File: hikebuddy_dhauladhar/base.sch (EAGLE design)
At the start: 114 parts, among them J1 MF-CON-MICROUSB-RIGHT, J2 GPS Port, J5 SOLDER_PAD_2, J9 47352-1001, U1 LTC3586EUFE-1#PBF, U2 MAX17260SETD+, U3 MF-DSC-SOT233-MMBT3904, U4 MF-DSC-SOT233-MMBT3904, U5 DRV2605LTDGSRQ1, U6 BMX160

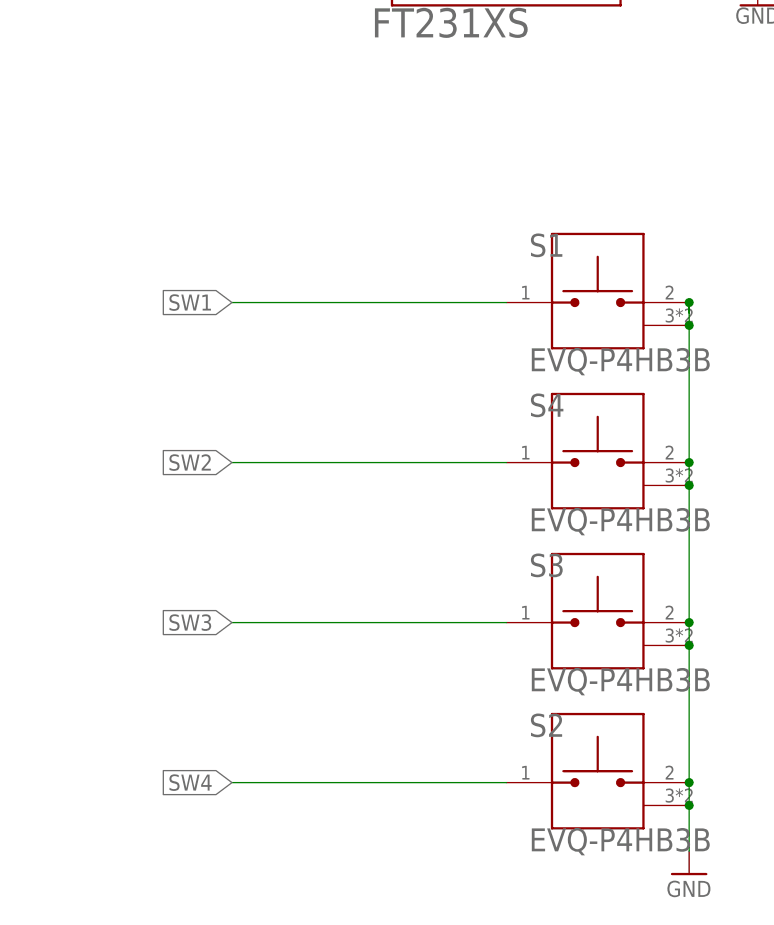
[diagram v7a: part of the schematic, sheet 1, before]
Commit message: added pullups to buttons, moved jst2 to make room for connector, removed test pads and joined EN to Vreg
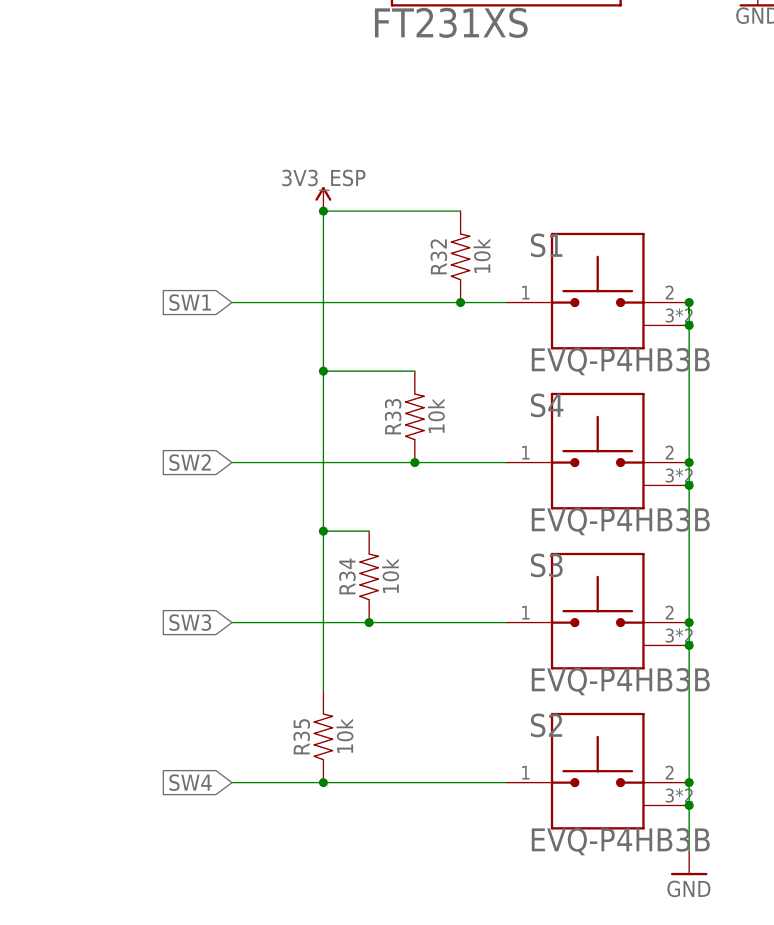
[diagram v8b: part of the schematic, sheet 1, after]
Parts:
- removed TP1, TP2: TEST-POINT2, SparkFun-Connectors:TEST-POINT2
- added R32, R33, R34, R35: 10k, SparkFun-Resistors:10KOHM-0603-1/10W-1%
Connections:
- removed net N$24: C20.P$2, R16.P$2, TP1.1, U1.FAULT
- net N$19: now also C20.P$2, R16.P$2, U1.FAULT; no longer TP2.1
- net SW1: now also R32.1
- net SW2: now also R33.1
- net SW3: now also R34.1
- net SW4: now also R35.1
- net VCC: now also R32.2, R33.2, R34.2, R35.2
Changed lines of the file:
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@@
 <part name="S1" library="EVQ-P4HB3B" deviceset="EVQ-P4HB3B" device="" override_package3d_urn="urn:adsk.eagle:package:16346036/2" override_package_urn="urn:adsk.eagle:footprint:16346037/1" override_locally_modified="yes"/>
 <part name="GND9" library="supply1" library_urn="urn:adsk.eagle:library:371" deviceset="GND" device=""/>
-<part name="TP1" library="SparkFun-Connectors" deviceset="TEST-POINT" device="2"/>
-<part name="TP2" library="SparkFun-Connectors" deviceset="TEST-POINT" device="2"/>
 <part name="J9" library="47352-1001" deviceset="47352-1001" device="" package3d_urn="urn:adsk.eagle:package:16346114/2"/>
+<part name="R32" library="SparkFun-Resistors" deviceset="10KOHM" device="-0603-1/10W-1%" package3d_urn="urn:adsk.eagle:package:23555/3" value="10k"/>
+<part name="R33" library="SparkFun-Resistors" deviceset="10KOHM" device="-0603-1/10W-1%" package3d_urn="urn:adsk.eagle:package:23555/3" value="10k"/>
+<part name="R34" library="SparkFun-Resistors" deviceset="10KOHM" device="-0603-1/10W-1%" package3d_urn="urn:adsk.eagle:package:23555/3" value="10k"/>
+<part name="R35" library="SparkFun-Resistors" deviceset="10KOHM" device="-0603-1/10W-1%" package3d_urn="urn:adsk.eagle:package:23555/3" value="10k"/>
+<part name="3V3_ESP3" library="SparkFun-PowerSymbols" library_urn="urn:adsk.eagle:library:530" deviceset="VCC" device="" value="3V3_ESP"/>
 </parts>
 <sheets>
@@
 <attribute name="NAME" x="350.52" y="168.402" size="1.778" layer="95"/>
 <attribute name="VALUE" x="350.52" y="134.62" size="1.778" layer="96"/>
+</instance>
+<instance part="R32" gate="G$1" x="53.34" y="27.94" smashed="yes" rot="R90">
+<attribute name="NAME" x="51.816" y="27.94" size="1.778" layer="95" font="vector" rot="R90" align="bottom-center"/>
+<attribute name="VALUE" x="54.864" y="27.94" size="1.778" layer="96" font="vector" rot="R90" align="top-center"/>
+</instance>
+<instance part="R33" gate="G$1" x="48.26" y="10.16" smashed="yes" rot="R90">
+<attribute name="NAME" x="46.736" y="10.16" size="1.778" layer="95" font="vector" rot="R90" align="bottom-center"/>
+<attribute name="VALUE" x="49.784" y="10.16" size="1.778" layer="96" font="vector" rot="R90" align="top-center"/>
+</instance>
+<instance part="R34" gate="G$1" x="43.18" y="-7.62" smashed="yes" rot="R90">
+<attribute name="NAME" x="41.656" y="-7.62" size="1.778" layer="95" font="vector" rot="R90" align="bottom-center"/>
+<attribute name="VALUE" x="44.704" y="-7.62" size="1.778" layer="96" font="vector" rot="R90" align="top-center"/>
+</instance>
+<instance part="R35" gate="G$1" x="38.1" y="-25.4" smashed="yes" rot="R90">
+<attribute name="NAME" x="36.576" y="-25.4" size="1.778" layer="95" font="vector" rot="R90" align="bottom-center"/>
+<attribute name="VALUE" x="39.624" y="-25.4" size="1.778" layer="96" font="vector" rot="R90" align="top-center"/>
+</instance>
+<instance part="3V3_ESP3" gate="G$1" x="38.1" y="33.02" smashed="yes">
+<attribute name="VALUE" x="38.1" y="35.814" size="1.778" layer="96" align="bottom-center"/>
 </instance>
 </instances>
@@
 <pinref part="C21" gate="G$1" pin="1"/>
 <junction x="403.86" y="114.3"/>
+</segment>
+<segment>
+<pinref part="R35" gate="G$1" pin="2"/>
+<wire x1="38.1" y1="-20.32" x2="38.1" y2="-2.54" width="0.1524" layer="91"/>
+<pinref part="R32" gate="G$1" pin="2"/>
+<wire x1="38.1" y1="-2.54" x2="38.1" y2="15.24" width="0.1524" layer="91"/>
+<wire x1="38.1" y1="15.24" x2="38.1" y2="33.02" width="0.1524" layer="91"/>
+<wire x1="38.1" y1="33.02" x2="53.34" y2="33.02" width="0.1524" layer="91"/>
+<pinref part="R33" gate="G$1" pin="2"/>
+<wire x1="48.26" y1="15.24" x2="38.1" y2="15.24" width="0.1524" layer="91"/>
+<junction x="38.1" y="15.24"/>
+<pinref part="R34" gate="G$1" pin="2"/>
+<wire x1="43.18" y1="-2.54" x2="38.1" y2="-2.54" width="0.1524" layer="91"/>
+<junction x="38.1" y="-2.54"/>
+<pinref part="3V3_ESP3" gate="G$1" pin="VCC"/>
+<junction x="38.1" y="33.02"/>
 </segment>
 </net>
@@
 <net name="SW1" class="0">
 <segment>
-<wire x1="58.42" y1="22.86" x2="27.94" y2="22.86" width="0.1524" layer="91"/>
+<wire x1="58.42" y1="22.86" x2="53.34" y2="22.86" width="0.1524" layer="91"/>
 <label x="27.94" y="22.86" size="1.778" layer="95" rot="R180" xref="yes"/>
 <pinref part="S1" gate="G$1" pin="1"/>
+<pinref part="R32" gate="G$1" pin="1"/>
+<wire x1="53.34" y1="22.86" x2="27.94" y2="22.86" width="0.1524" layer="91"/>
+<junction x="53.34" y="22.86"/>
 </segment>
 <segment>
@@
 <net name="SW2" class="0">
 <segment>
-<wire x1="58.42" y1="5.08" x2="27.94" y2="5.08" width="0.1524" layer="91"/>
+<wire x1="58.42" y1="5.08" x2="48.26" y2="5.08" width="0.1524" layer="91"/>
 <label x="27.94" y="5.08" size="1.778" layer="95" rot="R180" xref="yes"/>
 <pinref part="S4" gate="G$1" pin="1"/>
+<pinref part="R33" gate="G$1" pin="1"/>
+<wire x1="48.26" y1="5.08" x2="27.94" y2="5.08" width="0.1524" layer="91"/>
+<junction x="48.26" y="5.08"/>
 </segment>
 <segment>
@@
 <net name="SW3" class="0">
 <segment>
-<wire x1="58.42" y1="-12.7" x2="27.94" y2="-12.7" width="0.1524" layer="91"/>
+<wire x1="58.42" y1="-12.7" x2="43.18" y2="-12.7" width="0.1524" layer="91"/>
 <label x="27.94" y="-12.7" size="1.778" layer="95" rot="R180" xref="yes"/>
 <pinref part="S3" gate="G$1" pin="1"/>
+<pinref part="R34" gate="G$1" pin="1"/>
+<wire x1="43.18" y1="-12.7" x2="27.94" y2="-12.7" width="0.1524" layer="91"/>
+<junction x="43.18" y="-12.7"/>
 </segment>
 <segment>
@@
 <net name="SW4" class="0">
 <segment>
-<wire x1="58.42" y1="-30.48" x2="27.94" y2="-30.48" width="0.1524" layer="91"/>
+<wire x1="58.42" y1="-30.48" x2="38.1" y2="-30.48" width="0.1524" layer="91"/>
 <label x="27.94" y="-30.48" size="1.778" layer="95" rot="R180" xref="yes"/>
 <pinref part="S2" gate="G$1" pin="1"/>
+<pinref part="R35" gate="G$1" pin="1"/>
+<wire x1="38.1" y1="-30.48" x2="27.94" y2="-30.48" width="0.1524" layer="91"/>
+<junction x="38.1" y="-30.48"/>
 </segment>
 <segment>
@@
 <attribute name="NAME" x="48.26" y="64.516" size="1.016" layer="95" font="vector" rot="R180" align="top-left"/>
 <attribute name="VALUE" x="48.26" y="67.564" size="1.016" layer="96" font="vector" rot="R180"/>
-</instance>
-<instance part="TP1" gate="G$1" x="78.74" y="88.9" smashed="yes">
-<attribute name="NAME" x="76.2" y="91.44" size="1.778" layer="95" font="vector"/>
-<attribute name="VALUE" x="76.2" y="86.36" size="1.778" layer="96" font="vector"/>
-</instance>
-<instance part="TP2" gate="G$1" x="86.36" y="88.9" smashed="yes" rot="R180">
-<attribute name="NAME" x="88.9" y="86.36" size="1.778" layer="95" font="vector" rot="R180"/>
-<attribute name="VALUE" x="88.9" y="91.44" size="1.778" layer="96" font="vector" rot="R180"/>
 </instance>
 </instances>
@@
 </segment>
 </net>
-<net name="N$24" class="0">
-<segment>
+<net name="N$19" class="0">
+<segment>
+<pinref part="U1" gate="G$1" pin="EN3"/>
+<pinref part="U1" gate="G$1" pin="FAULT"/>
 <wire x1="78.74" y1="88.9" x2="78.74" y2="83.82" width="0.1524" layer="91"/>
-<pinref part="U1" gate="G$1" pin="FAULT"/>
 <wire x1="78.74" y1="83.82" x2="58.42" y2="83.82" width="0.1524" layer="91"/>
 <pinref part="R16" gate="G$1" pin="P$2"/>
@@
 <wire x1="53.34" y1="83.82" x2="50.8" y2="83.82" width="0.1524" layer="91"/>
 <junction x="53.34" y="83.82"/>
-<pinref part="TP1" gate="G$1" pin="1"/>
-</segment>
-</net>
-<net name="N$19" class="0">
-<segment>
-<pinref part="U1" gate="G$1" pin="EN3"/>
-<pinref part="TP2" gate="G$1" pin="1"/>
-<wire x1="86.36" y1="88.9" x2="93.98" y2="88.9" width="0.1524" layer="91"/>
-</segment>
-</net>
+<wire x1="93.98" y1="88.9" x2="78.74" y2="88.9" width="0.1524" layer="91"/>
+</segment>
+</net>
